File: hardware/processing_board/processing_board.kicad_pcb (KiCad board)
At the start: 2 copper layers, 155 parts, among them IC1 XC7S25-2CSGA225I, J1 USB_C_Receptacle_USB2.0_14P, J2 USB_C_Receptacle_USB2.0_14P, J3 S2B-PH-K-S_LF__SN_, J4 Conn_02x07_Counter_Clockwise, SW1 SW_Push, SW2 BOOT_BTN, SW3 RST_BTN, U1 BQ24075RGT, U10 MAX98357A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

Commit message: Routed charging circuit
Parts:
- added MT1: MountingHole_2.1mm, MountingHole:MountingHole_2.1mm, F.Cu at (83.5, 46.7)
- added MT2: MountingHole_2.1mm, MountingHole:MountingHole_2.1mm, F.Cu at (195.9, 46.7)
- added MT3: MountingHole_2.1mm, MountingHole:MountingHole_2.1mm, F.Cu at (195.9, 105.7)
- added MT4: MountingHole_2.1mm, MountingHole:MountingHole_2.1mm, F.Cu at (83.5, 105.7)
- added TP1: 5V, TestPoint:TestPoint_Loop_D2.60mm_Drill0.9mm_Beaded, F.Cu at (-76.2, -0.42)
- added TP10: CCLK_0, TestPoint:TestPoint_Loop_D2.60mm_Drill0.9mm_Beaded, F.Cu at (-71.2, 19.8)
- added TP11: 12MHZ, TestPoint:TestPoint_Loop_D2.60mm_Drill0.9mm_Beaded, F.Cu at (-66.1, -0.42)
- added TP12: Crystal, TestPoint:TestPoint_Loop_D2.60mm_Drill0.9mm_Beaded, F.Cu at (-66.1, 4.63)
- added TP13: ESP_RX, TestPoint:TestPoint_Loop_D2.60mm_Drill0.9mm_Beaded, F.Cu at (-66.1, 9.68)
- added TP14: ESP_TX, TestPoint:TestPoint_Loop_D2.60mm_Drill0.9mm_Beaded, F.Cu at (-66.1, 14.7)
- added TP2: 3V3, TestPoint:TestPoint_Loop_D2.60mm_Drill0.9mm_Beaded, F.Cu at (-76.2, 4.63)
- added TP3: 1V0, TestPoint:TestPoint_Loop_D2.60mm_Drill0.9mm_Beaded, F.Cu at (-76.2, 9.68)
- added TP4: 1V8, TestPoint:TestPoint_Loop_D2.60mm_Drill0.9mm_Beaded, F.Cu at (-76.2, 14.7)
- added TP5: 3.3V, TestPoint:TestPoint_Loop_D2.60mm_Drill0.9mm_Beaded, F.Cu at (-76.2, 19.8)
- added TP6: GND, TestPoint:TestPoint_Loop_D2.60mm_Drill0.9mm_Beaded, F.Cu at (-71.2, -0.42)
- added TP7: DONE_0, TestPoint:TestPoint_Loop_D2.60mm_Drill0.9mm_Beaded, F.Cu at (-71.2, 4.63)
- added TP8: PROGRAM_B, TestPoint:TestPoint_Loop_D2.60mm_Drill0.9mm_Beaded, F.Cu at (-71.2, 9.68)
- added TP9: INIT_B, TestPoint:TestPoint_Loop_D2.60mm_Drill0.9mm_Beaded, F.Cu at (-71.2, 14.7)
- C10: footprint Capacitor_SMD:C_0805_2012Metric -> Resistor_SMD:R_0402_1005Metric
- R6, R7: footprint Resistor_SMD:R_0805_2012Metric -> Resistor_SMD:R_0402_1005Metric
- moved C1 175.8 mm to (89.6, 77.0)
- moved X1 173.3 mm to (100.5, 50.3)
- moved R2 171.2 mm to (89.5, 81.9)
- moved R1 170.5 mm to (89.5, 78.7)
- moved R20 164.5 mm to (99.4, 70.5), turned to 180 degrees
- moved R18 161.8 mm to (96.4, 66.4), turned to 90 degrees
- moved R19 158.4 mm to (92.6, 68.4), turned to 90 degrees
- moved J3 154.2 mm to (86.0, 68.6), turned to -90 degrees
- moved J2 153.2 mm to (83.7, 94.2), turned to -90 degrees
- moved D2 151.3 mm to (99.4, 72.2)
- moved J1 151.1 mm to (83.7, 80.5), turned to -90 degrees
- moved C2 148.9 mm to (90.4, 75.4)
- moved R6 147.0 mm to (98.7, 68.4), turned to 90 degrees
- moved R7 141.5 mm to (94.1, 66.9), turned to 180 degrees
- moved C10 140.2 mm to (89.2, 70.6), turned to -90 degrees
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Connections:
- J3 pad 1: /<NO NET> -> GND
- J3 pad 2: GND -> /<NO NET>
- R15 pad 1: +3V3 -> +3.3V
- U6 pad 50: +3V3 -> +3.3V
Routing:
- net +5V: track 0.00 -> 21.4 mm, vias 0 -> 2
- net GND: track 0.00 -> 17.2 mm, vias 0 -> 21
- net /SYS: track 0.00 -> 9.72 mm, vias 0 -> 2
- net /<NO NET>: track 0.00 -> 9.04 mm
- net /ESP_D-: track 0.00 -> 5.43 mm, vias 0 -> 1
- net /ESP_D+: track 0.00 -> 2.62 mm, vias 0 -> 1
- net Net-(J1-CC2): track 0.00 -> 2.33 mm
- net Net-(J1-CC1): track 0.00 -> 2.31 mm
- net Net-(D2-K): track 0.00 -> 2.13 mm
- net Net-(D2-A): track 0.00 -> 2.02 mm
- net Net-(U1-TMR): track 0.00 -> 1.82 mm
- net Net-(U1-ISET): track 0.00 -> 1.72 mm
- net Net-(U1-ILIM): track 0.00 -> 1.72 mm
- net Net-(U1-TS): track 0.00 -> 1.72 mm
- added copper zone on In2.Cu, net +3V3
- added copper zone on In1.Cu, net GND
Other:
- board outline added: 122.3 x 69 mm
- copper layers 2 -> 4

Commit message: Added 1V0 buck circuit
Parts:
- added C83: 0.1uF, Capacitor_SMD:C_0402_1005Metric, B.Cu at (107.1, 79.9)
- moved TP3 198.9 mm to (110.8, 77.5)
- moved TP2 191.9 mm to (102.1, 75.4)
- moved TP1 188.2 mm to (90.4, 87.1)
- moved C6 185.4 mm to (96.8, 77.0), turned to 180 degrees
- moved R9 183.5 mm to (107.4, 83.7), turned to 180 degrees
- moved R10 180.8 mm to (105.4, 83.7), turned to 180 degrees
- moved D1 180.5 mm to (94.2, 90.2), turned to 180 degrees
- moved L1 180.3 mm to (109.3, 81.4)
- moved R8 179.1 mm to (104.1, 78.6), turned to -90 degrees
- moved R3 178.8 mm to (89.4, 95.8)
- moved R5 175.8 mm to (93.5, 88.4)
- moved R4 175.6 mm to (89.4, 92.2)
- moved U3 175.5 mm to (105.4, 81.2)
- moved R42 173.0 mm to (106.6, 78.6), turned to -90 degrees
- moved C7 161.5 mm to (110.1, 84.5), turned to -90 degrees
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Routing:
- net +3V3: track 0.00 -> 26.6 mm, vias 0 -> 6
- net GND: track 17.2 -> 29.4 mm, vias 21 -> 37
- net /SYS: track 9.72 -> 21.5 mm
- net +1V0: track 0.00 -> 10.6 mm
- net +5V: track 21.4 -> 31.7 mm
- net Net-(U3-FB): track 0.00 -> 4.95 mm
- net Net-(U3-SW): track 0.00 -> 2.35 mm
- net Net-(J2-CC2): track 0.00 -> 2.29 mm
- net Net-(J2-CC1): track 0.00 -> 2.23 mm
- net Net-(D1-A): track 0.00 -> 2.06 mm
- net Net-(U3-EN): track 0.00 -> 1.54 mm
- net /1V0_PG: track 0.00 -> 1.50 mm

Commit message: Added 1V8 LDO circuit
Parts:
- moved TP4 195.5 mm to (110.0, 74.4)
- moved C12 193.1 mm to (110.0, 78.8), turned to -90 degrees
- moved C11 189.0 mm to (103.9, 78.9), turned to -90 degrees
- moved R11 185.2 mm to (113.6, 78.8), turned to -90 degrees
- moved U11 179.4 mm to (106.9, 79.4)
- moved C82 178.8 mm to (110.0, 81.2), turned to -90 degrees
- moved C14 163.5 mm to (115.4, 78.1), turned to 90 degrees
- moved C13 158.7 mm to (111.9, 79.6), turned to -90 degrees
- moved TP3 7.01 mm to (113.8, 83.8)
- moved C83 4.20 mm to (107.4, 84.1)
- moved L1 4.20 mm to (109.6, 85.6)
- moved R42 4.20 mm to (106.9, 82.8)
- moved R8 4.20 mm to (104.3, 82.8)
- moved R9 4.20 mm to (107.6, 87.9)
- moved R10 4.20 mm to (105.6, 87.9)
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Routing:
- net +1V8: track 0.00 -> 9.83 mm
- net GND: track 29.4 -> 33.9 mm, vias 37 -> 41
- net /1V0_PG: track 1.50 -> 4.89 mm
- net +3V3: track 26.6 -> 29.0 mm, vias 6 -> 7
- net Net-(U11-BP): track 0.00 -> 2.07 mm
- net /3V3_PG: track 0.00 -> 1.88 mm

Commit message: Added 3.3V FPGA rail LDO
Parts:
- moved C9 197.5 mm to (105.2, 90.2), turned to -90 degrees
- moved TP5 197.0 mm to (106.2, 94.2)
- moved C8 193.8 mm to (99.1, 90.2), turned to -90 degrees
- moved U4 181.3 mm to (102.1, 90.7)
- moved R10 14.9 mm to (113.4, 75.2), turned to 0 degrees
- moved C7 14.4 mm to (108.7, 74.4), turned to 90 degrees
- moved TP4 14.3 mm to (109.1, 88.6), turned to 180 degrees
- moved C14 13.6 mm to (103.6, 85.0), turned to -90 degrees
- moved R9 13.2 mm to (111.4, 75.2), turned to 0 degrees
- moved C11 12.5 mm to (115.2, 84.1), turned to 90 degrees
- moved U3 10.9 mm to (113.4, 77.7), turned to 180 degrees
- moved R8 10.7 mm to (114.7, 80.3), turned to 90 degrees
- moved R11 9.88 mm to (105.4, 84.3), turned to 90 degrees
- moved TP3 9.69 mm to (105.2, 79.2), turned to 180 degrees
- moved L1 8.13 mm to (109.5, 77.5), turned to 180 degrees
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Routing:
- net /3V3_PG: track 1.88 -> 10.8 mm
- net +3.3V: track 0.00 -> 8.03 mm
- net GND: track 33.9 -> 36.9 mm, vias 41 -> 43
- net +3V3: track 29.0 -> 31.0 mm

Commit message: Added BOOT and RST btns for ESP32, routed flash
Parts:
- removed MT1: MountingHole_2.1mm, MountingHole:MountingHole_2.1mm
- C30, R12, R25, R26: moved to B.Cu
- moved R13 188.9 mm to (102.9, 96.4), turned to -90 degrees
- moved D4 185.3 mm to (101.0, 97.1), turned to 90 degrees
- moved D3 181.6 mm to (102.1, 83.8), turned to 90 degrees
- moved R12 180.9 mm to (102.1, 81.0), turned to -90 degrees
- moved C77 172.5 mm to (108.7, 61.7), turned to -90 degrees
- moved R33 168.5 mm to (106.7, 63.0)
- moved R35 165.3 mm to (108.7, 53.6), turned to 90 degrees
- moved C30 164.4 mm to (84.4, 68.3)
- moved R34 163.1 mm to (106.0, 52.3)
- moved R26 155.9 mm to (97.5, 48.8), turned to 180 degrees
- moved R25 152.1 mm to (84.3, 67.1), turned to 180 degrees
- moved SW2 145.8 mm to (105.2, 46.5), turned to 180 degrees
- moved SW3 145.4 mm to (105.2, 50.0), turned to 180 degrees
- moved U9 136.1 mm to (105.4, 57.7), turned to -90 degrees
- moved X1 13.6 mm to (87.8, 55.2), turned to 90 degrees
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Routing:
- net /EN: track 0.00 -> 31.5 mm, vias 0 -> 3
- net GND: track 36.9 -> 63.4 mm, vias 43 -> 58
- net /ESP_D+: track 2.62 -> 28.5 mm, vias 1 -> 2
- net /ESP_D-: track 5.43 -> 30.4 mm, vias 1 -> 2
- net +3V3: track 31.0 -> 46.1 mm, vias 7 -> 13
- net /MAX_DIN: track 0.00 -> 11.2 mm
- net /ESP_CS: track 0.00 -> 10.7 mm
- net /MAX_BCLK: track 0.00 -> 9.99 mm
- net /ESP_CLK: track 0.00 -> 8.40 mm, vias 0 -> 2
- net /MAX_LRCLK: track 0.00 -> 8.07 mm
- net /BOOT: track 0.00 -> 7.08 mm, vias 0 -> 1
- net /ESP_DO: track 0.00 -> 6.93 mm
- net /ESP_DI: track 0.00 -> 6.75 mm, vias 0 -> 2
- net /MAX_SDMODE: track 0.00 -> 6.43 mm
- net +3.3V: track 8.03 -> 11.7 mm
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
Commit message: Routed audio amplifier and speaker jack
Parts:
- moved C29 191.6 mm to (123.0, 54.4), turned to 90 degrees
- moved R24 181.4 mm to (119.5, 58.8), turned to 90 degrees
- moved U10 176.0 mm to (119.9, 55.3), turned to 90 degrees
- moved LS1 156.9 mm to (121.4, 49.3), turned to 180 degrees
- moved SW2 3.43 mm to (108.6, 46.4)
- moved SW3 3.43 mm to (108.6, 49.9)
- moved U9 2.99 mm to (108.3, 58.3)
- moved R33 2.99 mm to (109.6, 63.6)
- moved C77 2.99 mm to (111.6, 62.4)
- moved R35 2.99 mm to (111.6, 54.2)
- moved R34 2.44 mm to (108.5, 52.7)
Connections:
- net Net-(U10-OUTN) renamed U10-
- net Net-(U10-OUTP) renamed U10+
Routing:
- net /MAX_SDMODE: track 6.43 -> 41.4 mm, vias 0 -> 2
- net /MAX_DIN: track 11.2 -> 45.4 mm, vias 0 -> 3
- net /MAX_BCLK: track 9.99 -> 42.8 mm, vias 0 -> 3
- net /MAX_LRCLK: track 8.07 -> 40.7 mm, vias 0 -> 2
- net U10+: track 0.00 -> 4.95 mm
- net U10-: track 0.00 -> 4.95 mm
- net GND: track 63.4 -> 68.0 mm, vias 58 -> 62
- net +3V3: track 46.1 -> 49.9 mm, vias 13 -> 15
- net /ESP_CLK: track 8.40 -> 11.9 mm
- net /BOOT: track 7.08 -> 10.6 mm
- net /EN: track 31.5 -> 35.0 mm
- net /ESP_DI: track 6.75 -> 10.0 mm
- net /ESP_DO: track 6.93 -> 9.80 mm
- net /ESP_CS: track 10.7 -> 13.3 mm
- net Net-(U10-GAIN_SLOT): track 0.00 -> 1.61 mm

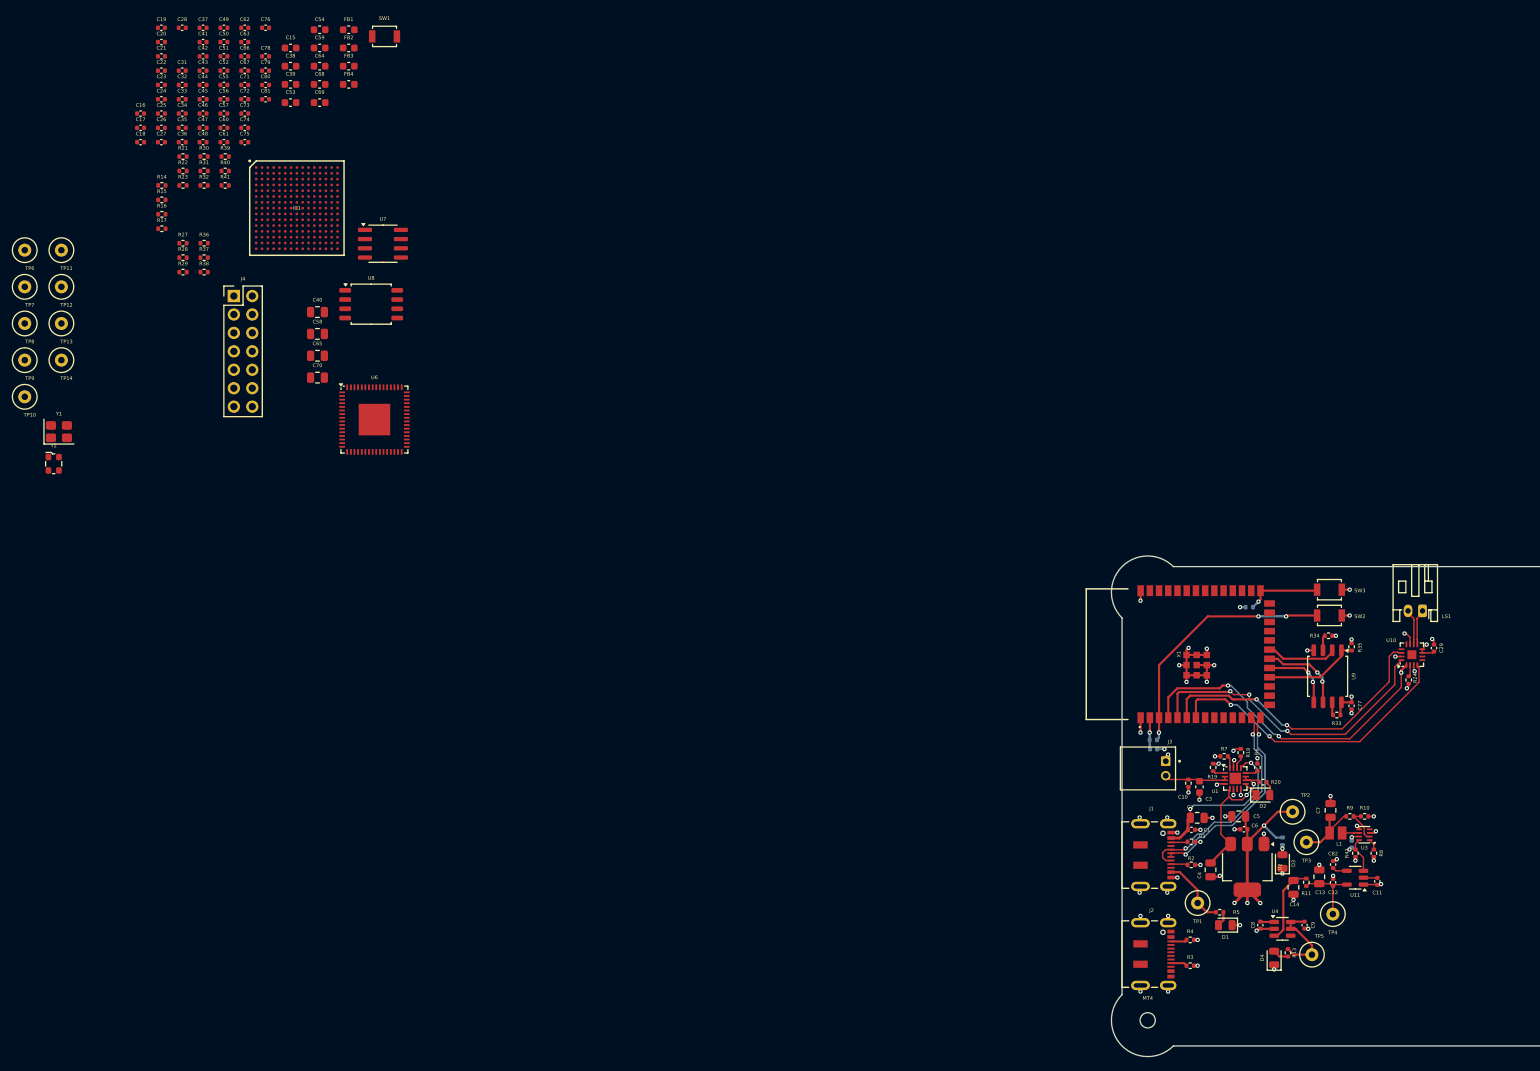
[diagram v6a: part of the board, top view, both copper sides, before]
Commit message: Added routed USB-C to JTAG bridge
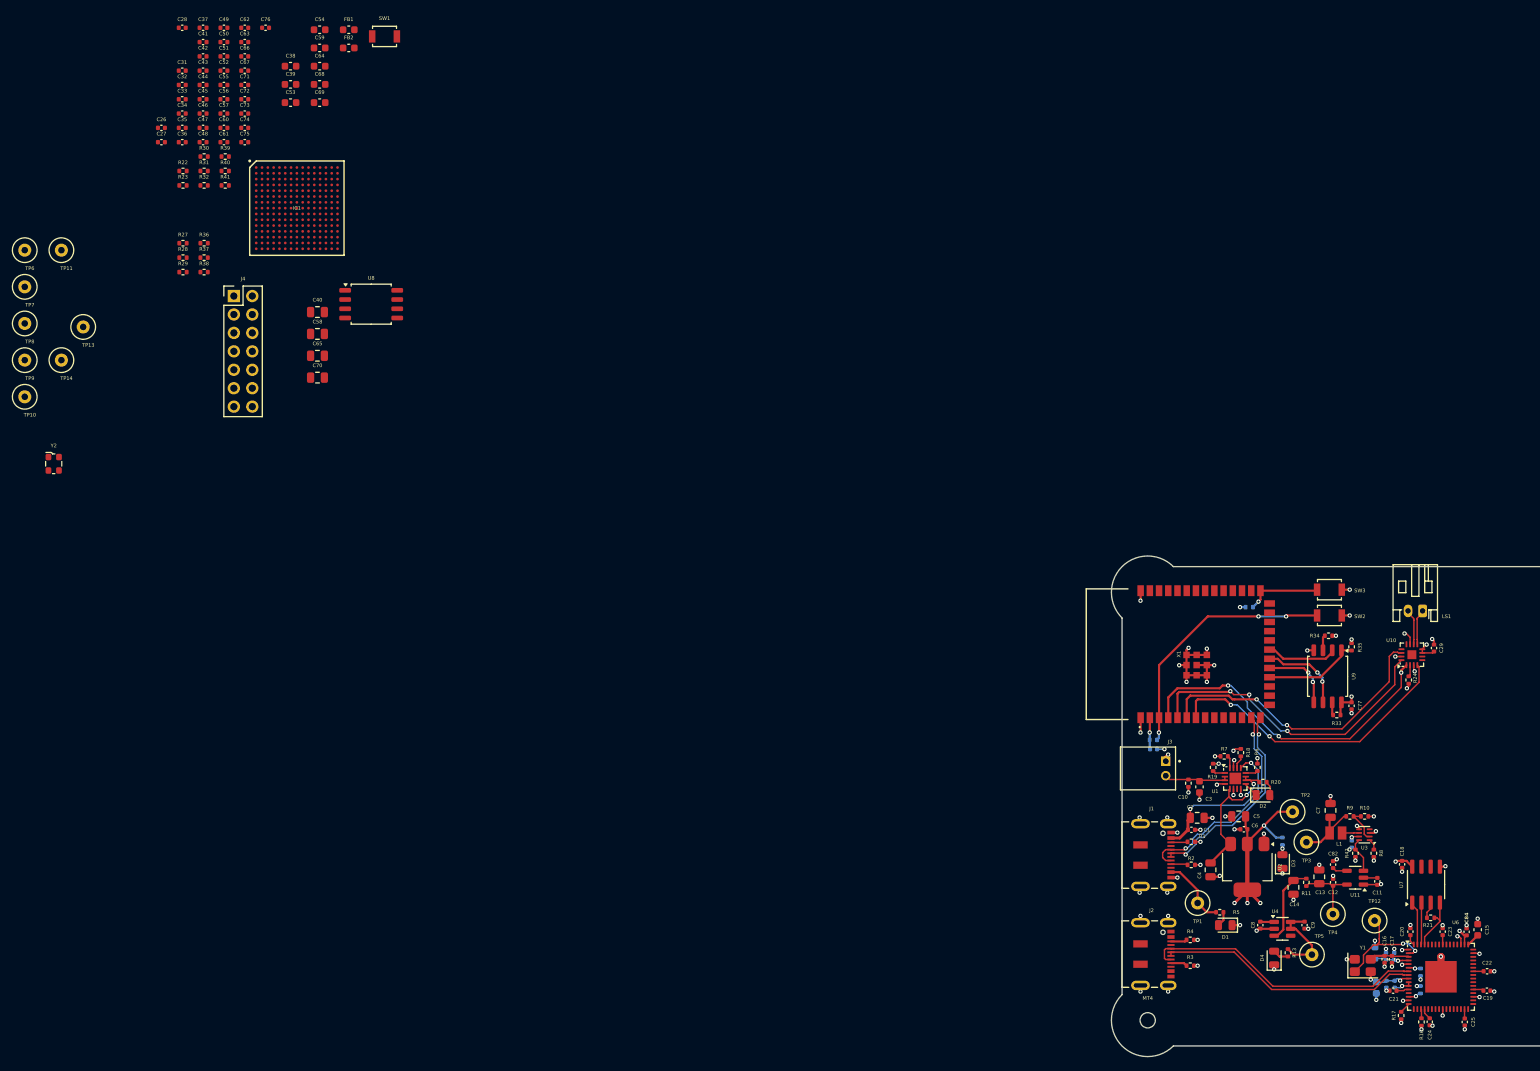
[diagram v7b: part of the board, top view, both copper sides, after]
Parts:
- added C84: 0.1uF, Capacitor_SMD:C_0402_1005Metric, F.Cu at (127.5, 93.5)
- C78, C79, C80, C81, FB3, FB4, R14, R15: moved to B.Cu
- moved C19 225.7 mm to (130.3, 101.6)
- moved C22 220.8 mm to (130.3, 98.9)
- moved C25 218.9 mm to (127.2, 105.9), turned to -90 degrees
- moved C24 216.1 mm to (122.4, 105.9), turned to -90 degrees
- moved C21 213.0 mm to (117.4, 101.6), turned to 180 degrees
- moved C23 211.6 mm to (124.2, 93.5), turned to 90 degrees
- moved C20 211.3 mm to (119.7, 93.5), turned to 90 degrees
- moved C16 207.3 mm to (116.2, 97.3), turned to -90 degrees
- moved C17 207.0 mm to (117.2, 97.3), turned to -90 degrees
- moved R16 206.2 mm to (121.3, 105.9), turned to -90 degrees
- moved R15 204.7 mm to (121.1, 101.5), turned to -90 degrees
- moved R14 204.5 mm to (121.1, 99.1), turned to 90 degrees
- moved C15 203.7 mm to (129.0, 93.2), turned to 90 degrees
- moved R17 202.3 mm to (118.5, 105.0), turned to -90 degrees
- moved R21 201.4 mm to (122.5, 91.6)
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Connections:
- IC1 pad K5: +3.3V -> /TMS
- LS1 pad 1: U10+ -> Net-(U10-OUTP)
- LS1 pad 2: U10- -> Net-(U10-OUTN)
- R16 pad 1: Net-(U6-ADBUS3) -> /TMS
- U6 pad 19: Net-(U6-ADBUS3) -> /TMS
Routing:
- net /FPGA_D-: track 0.00 -> 38.9 mm
- net /FPGA_D+: track 0.00 -> 36.3 mm
- net GND: track 68.0 -> 91.7 mm, vias 62 -> 90
- net Net-(U6-OSCI): track 0.00 -> 15.7 mm, vias 0 -> 2
- net Net-(U6-EEDATA): track 0.00 -> 7.56 mm
- net /EECS: track 0.00 -> 6.06 mm
- net /EECLK: track 0.00 -> 5.80 mm
- net /VCCIO: track 0.00 -> 5.60 mm
- net Net-(U6-OSCO): track 0.00 -> 5.48 mm
- net +3.3V: track 11.7 -> 17.1 mm, vias 0 -> 5
- net /VPHY: track 0.00 -> 5.25 mm, vias 0 -> 1
- net /VPLL: track 0.00 -> 4.88 mm, vias 0 -> 1
- net /VCORE: track 0.00 -> 4.68 mm
- net +3V3: track 49.9 -> 52.6 mm, vias 15 -> 16
- net Net-(U7-DI): track 0.00 -> 2.31 mm
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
